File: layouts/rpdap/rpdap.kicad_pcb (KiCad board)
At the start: 4 copper layers, 56 parts

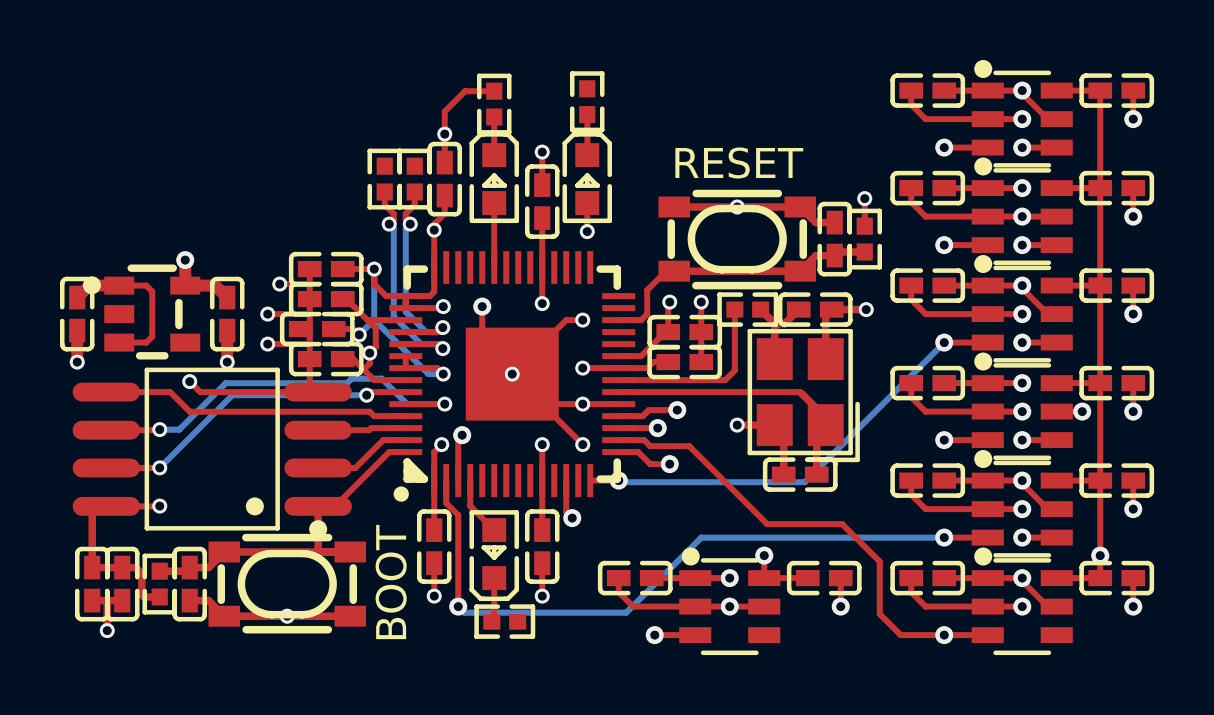
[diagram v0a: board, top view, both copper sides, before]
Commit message: rebuild with upstream rp2040 fixes. move header .25mm to the right. center dap-LED
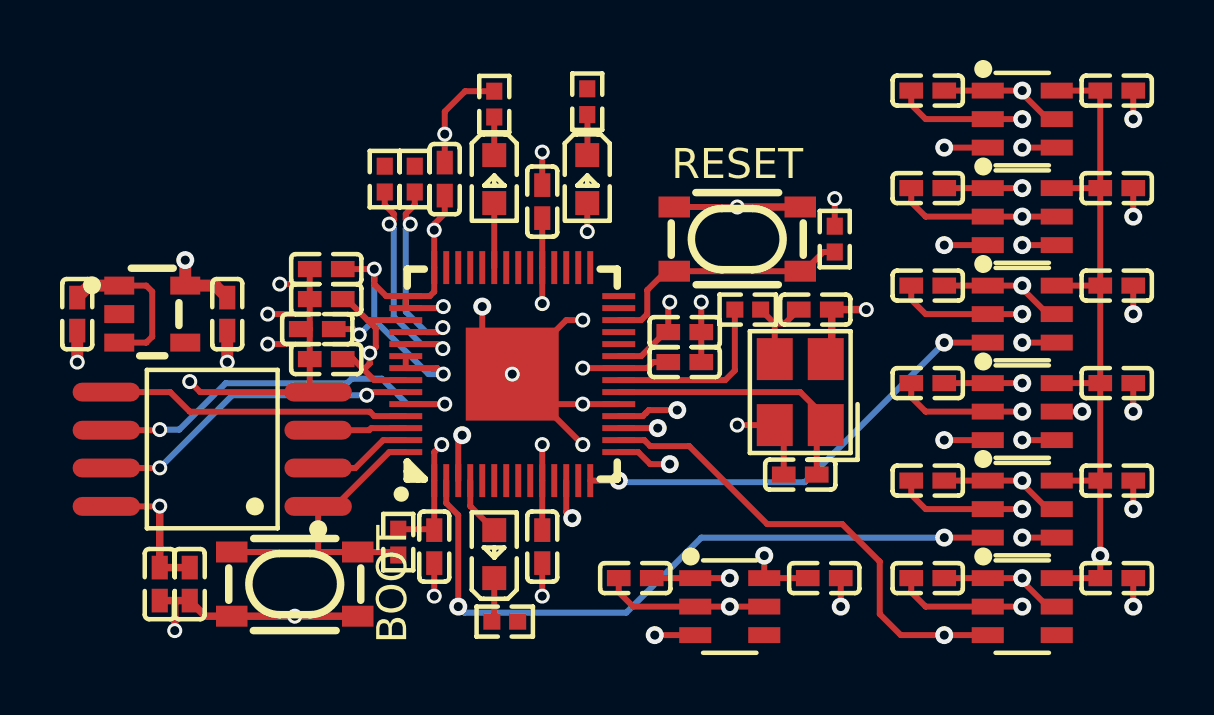
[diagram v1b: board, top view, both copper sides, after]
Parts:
- removed C15, C30: 1µF ±10% 25V X5R, Samsung_Electro_Mechanics_CL05A105KA5NQNC:C0402
- X1: footprint Yangxing_Tech_X322512MSB4SI:CRYSTAL-SMD_4P-L3.2-W2.5-BL -> Abracon_LLC_ABM8_272_T3:CRYSTAL-SMD_4P-L3.2-W2.5-BL
- moved R2 8.07 mm to (-3.80, 5.60)
- moved C29 2.25 mm to (-10.7, 7.00)
- moved C28 2.25 mm to (-11.8, 7.00)
- moved R5 1.00 mm to (10.7, -4.50), turned to 90 degrees
- moved SW1 0.25 mm to (-7.25, 7.00), turned to 0 degrees
- turned SW2 to 180 degrees
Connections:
- net RP_USB_N renamed output-USB_D_N
- net RP_USB_P renamed output-USB_D_P
- net USB_N renamed input-USB_D_N
- net USB_P renamed input-USB_D_P
- net anode renamed vcp_indicator-power-anode
- C11 pad 1: 3V3 -> qspi_flash-power-anode
- C13 pad 1: 3V3 -> qspi_flash-power-anode
- C2 pad 1: 3V3 -> qspi_flash-power-anode
- C21 pad 1: 3V3 -> qspi_flash-power-anode
- C22 pad 1: 3V3 -> qspi_flash-power-anode
- C23 pad 1: 3V3 -> qspi_flash-power-anode
- C24 pad 1: 3V3 -> qspi_flash-power-anode
- C25 pad 1: 3V3 -> qspi_flash-power-anode
- C26 pad 1: 3V3 -> qspi_flash-power-anode
- C27 pad 1: 3V3 -> qspi_flash-power-anode
- C28 pad 1: 3V3 -> qspi_flash-power-anode
- C29 pad 1: 3V3 -> qspi_flash-power-anode
- C3 pad 1: 3V3 -> qspi_flash-power-anode
- C31 pad 1: 3V3 -> qspi_flash-power-anode
- C5 pad 1: 3V3 -> qspi_flash-power-anode
- C7 pad 1: 3V3 -> qspi_flash-power-anode
- C9 pad 1: 3V3 -> qspi_flash-power-anode
- LED2 pad 2: 3V3 -> qspi_flash-power-anode
- R2 pad 1: 3V3 -> chip_select
- R2 pad 2: chip_select -> qspi_flash-power-anode
- R5 pad 1: 3V3 -> RUN
- R5 pad 2: RUN -> qspi_flash-power-anode
- SW1 pad 1: GND -> chip_select
- SW1 pad 2: GND -> chip_select
- SW1 pad 3: chip_select -> GND
- SW1 pad 4: chip_select -> GND
- SW2 pad 1: GND -> RUN
- SW2 pad 2: GND -> RUN
- SW2 pad 3: RUN -> GND
- SW2 pad 4: RUN -> GND
- U1 pad 5: 3V3 -> qspi_flash-power-anode
- U10 pad 1: 3V3 -> qspi_flash-power-anode
- U10 pad 5: GND -> (no net)
- U2 pad 1: 3V3 -> qspi_flash-power-anode
- U3 pad 1: 3V3 -> qspi_flash-power-anode
- U3 pad 5: 3V3 -> qspi_flash-power-anode
- U4 pad 1: 3V3 -> qspi_flash-power-anode
- U4 pad 5: GND -> (no net)
- U5 pad 1: 3V3 -> qspi_flash-power-anode
- U5 pad 5: 3V3 -> qspi_flash-power-anode
- U6 pad 1: 3V3 -> qspi_flash-power-anode
- U6 pad 5: 3V3 -> qspi_flash-power-anode
- U7 pad 1: 3V3 -> qspi_flash-power-anode
- U7 pad 5: 3V3 -> qspi_flash-power-anode
- U8 pad 1: 3V3 -> qspi_flash-power-anode
- U8 pad 10: 3V3 -> qspi_flash-power-anode
- U8 pad 22: 3V3 -> qspi_flash-power-anode
- U8 pad 33: 3V3 -> qspi_flash-power-anode
- U8 pad 42: 3V3 -> qspi_flash-power-anode
- U8 pad 43: 3V3 -> qspi_flash-power-anode
- U8 pad 44: 3V3 -> qspi_flash-power-anode
- U8 pad 48: 3V3 -> qspi_flash-power-anode
- U8 pad 49: 3V3 -> qspi_flash-power-anode
- U9 pad 8: 3V3 -> qspi_flash-power-anode
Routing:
- net GND: track 0.00 -> 94.1 mm, vias 0 -> 32
- net 3V3: track 64.7 -> 0.00 mm, vias 20 -> 0
- net (no net): track 95.3 -> 63.9 mm, vias 35 -> 23
- net chip_select: track 12.9 -> 10.8 mm
- net RUN: track 9.61 -> 8.61 mm

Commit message: fix swapped jlink connector pinout + update deps
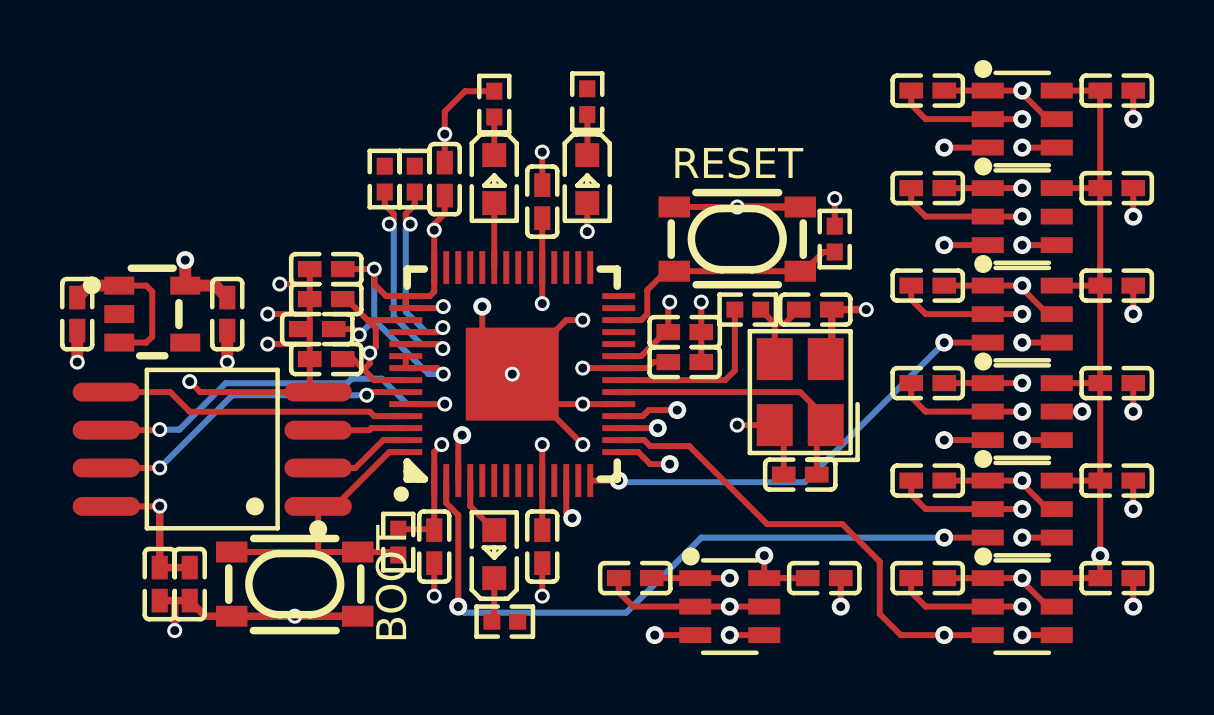
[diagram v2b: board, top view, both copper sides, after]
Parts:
- C16, C21, C28: value 2.2µF ±20% 6.3V X5R -> 2.2µF ±10% 16V X5R; footprint Samsung_Electro_Mechanics_CL05A225MQ5NSNC:C0402 -> Samsung_Electro_Mechanics_CL05A225KO5NQNC:C0402
- R6, R7: footprint YAGEO_RC0402FR_0727RL:R0402 -> UNI_ROYAL_0402WGF270JTCE:R0402
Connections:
- net A renamed input-A
- net _core_regulator_out_power-VCC renamed VCC
- net a-RX renamed uart-RX
- net a-TX renamed uart-TX
- net dir-line renamed DIR
- net model-a-line-0 renamed gpio[12]-A
- net model-a-line-1 renamed gpio[11]-A
- net model-a-line-2 renamed gpio[14]-A
- net model-a-line-3 renamed gpio[15]-A
- net model-a-line-4 renamed gpio[13]-A
- net power_shim-VCC renamed Vbus_fused
- net qspi_flash-power-anode renamed 3V3
- net vcp_indicator-power-anode renamed anode
- U10 pad 5: (no net) -> GND
- U4 pad 5: (no net) -> GND
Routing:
- net (no net): track 63.9 -> 0.00 mm, vias 23 -> 3
- net 3V3: track 0.00 -> 63.9 mm, vias 0 -> 20
- net b-RX: track 0.00 -> 1.15 mm, vias 0 -> 1
- net TDI: track 0.00 -> 1.15 mm, vias 0 -> 1
- net GND: track 94.1 -> 93.0 mm
